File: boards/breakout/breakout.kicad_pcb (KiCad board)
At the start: 2 copper layers, 111 x 56 mm, 12 parts, among them J1 8P8C_Shielded, J2 DE15_Receptacle_HighDensity_M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, J3 Conn_02x04_Odd_Even, J4 Conn_02x05_Odd_Even

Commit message: Rev1 hardware
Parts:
- R1, R2: footprint Resistor_SMD:R_0805_2012Metric_Pad1.20x1.40mm_HandSolder -> Resistor_THT:R_Axial_DIN0204_L3.6mm_D1.6mm_P7.62mm_Horizontal
- moved R1 6.19 mm to (65.7, 37.7)
- moved R2 6.19 mm to (68.3, 37.7)
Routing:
- net Net-(D2-A): track 36.8 -> 31.7 mm
- net Net-(D1-A): track 31.2 -> 26.0 mm
- net /LEDA: track 18.5 -> 17.4 mm
- net /LEDB: track 16.9 -> 16.3 mm

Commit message: update schematics
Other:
- board text added: "1 2 3 4 5 6 7 8 9 10"
- board text added: "10"
- board text added: "2"
- board text added: "9"
- board text added: "Red Red Ground Sense 1 Composite Sync Green Sense 0 NC Green Ground Blue Blue Ground"
- board text added: "SEthernet Breakout github.com/rhalkyard/SEThernet Revision 1"
- board text removed: "SEthernet Breakout github.com/rhalkyard/SEThernet Revision 0"
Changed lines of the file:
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@@
   (gr_rect (start 30.95 23.5) (end 141.95 79.5)
     (stroke (width 0.1) (type default)) (fill none) (layer "Edge.Cuts"))
-  (gr_text "SEthernet" (at 46.99 39.49) (layer "B.SilkS")
+  (gr_text "2" (at 118.834 26.167) (layer "B.SilkS")
     (effects (font (size 1 1) (thickness 0.15)) (justify bottom mirror))
   )
-  (gr_text "RasterOps ColorBoard 264" (at 116.84 39.49) (layer "B.SilkS")
+  (gr_text "1" (at 120.104 36.327) (layer "B.SilkS")
+    (effects (font (size 1 1) (thickness 0.15)) (justify top mirror))
+  )
+  (gr_text "10" (at 108.674 26.167) (layer "B.SilkS")
     (effects (font (size 1 1) (thickness 0.15)) (justify bottom mirror))
   )
-  (gr_text "SEthernet Breakout\ngithub.com/rhalkyard/SEThernet\nRevision 0" (at 36.665 24.89 90) (layer "B.SilkS")
+  (gr_text "SEthernet" (at 62.7 27.31) (layer "B.SilkS")
+    (effects (font (size 1 1) (thickness 0.2) bold) (justify right bottom mirror))
+  )
+  (gr_text "RasterOps ColorBoard 264" (at 102.07 27.31) (layer "B.SilkS")
+    (effects (font (size 1 1) (thickness 0.2) bold) (justify left bottom mirror))
+  )
+  (gr_text "Red\nRed Ground\nSense 1\nComposite Sync\nGreen\nSense 0\nNC\nGreen Ground\nBlue\nBlue Ground" (at 98.895 28.58) (layer "B.SilkS")
+    (effects (font (size 1 1) (thickness 0.15)) (justify left top mirror))
+  )
+  (gr_text "1\n2\n3\n4\n5\n6\n7\n8\n9\n10" (at 102.07 28.58) (layer "B.SilkS")
+    (effects (font (size 1 1) (thickness 0.15)) (justify left top mirror))
+  )
+  (gr_text "SEthernet Breakout\ngithub.com/rhalkyard/SEThernet\nRevision 1" (at 36.665 24.89 90) (layer "B.SilkS")
     (effects (font (size 1 1) (thickness 0.15)) (justify left bottom mirror))
   )
+  (gr_text "9" (at 108.674 36.327) (layer "B.SilkS")
+    (effects (font (size 1 1) (thickness 0.15)) (justify top mirror))
+  )
   (gr_text "Link" (at 67.909 63.714) (layer "F.SilkS")

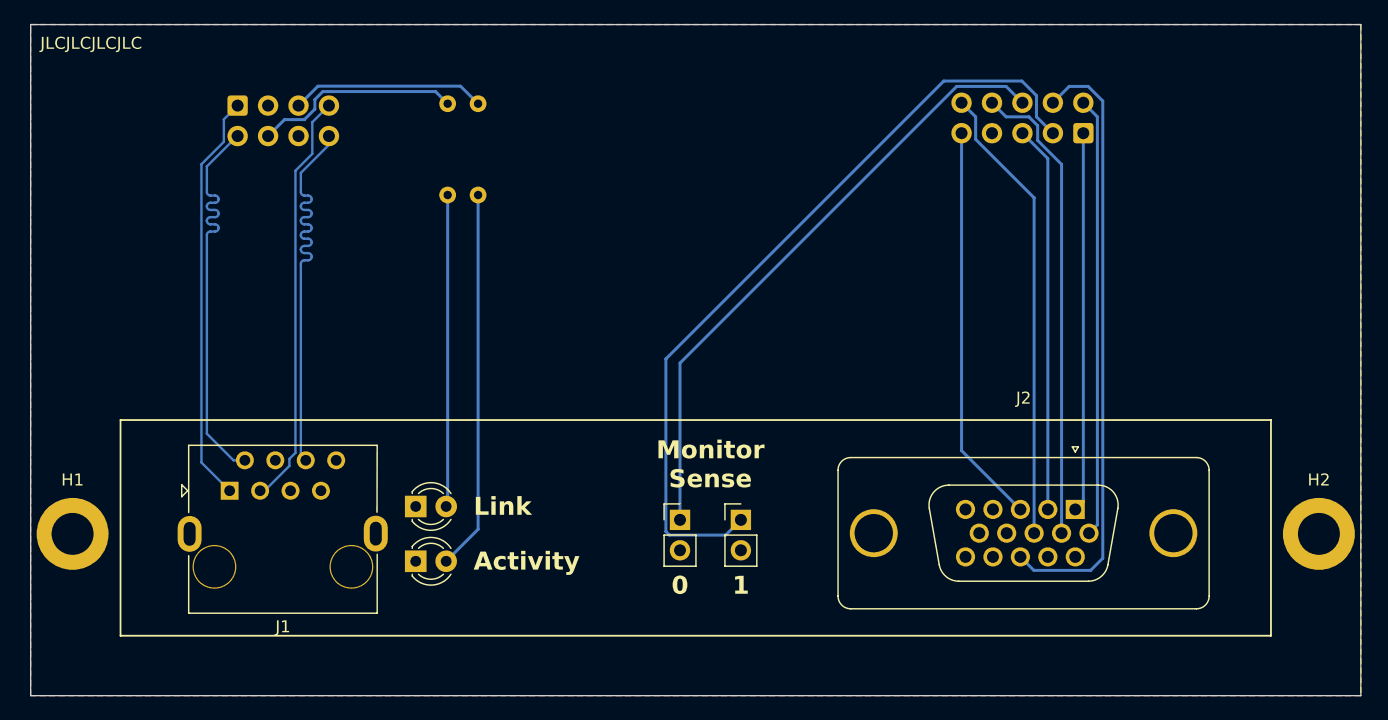
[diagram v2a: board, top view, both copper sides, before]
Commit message: Breakout: use threaded inserts for mounting
Resize mounting holes for use with Wurth 9774025360R threaded inserts.
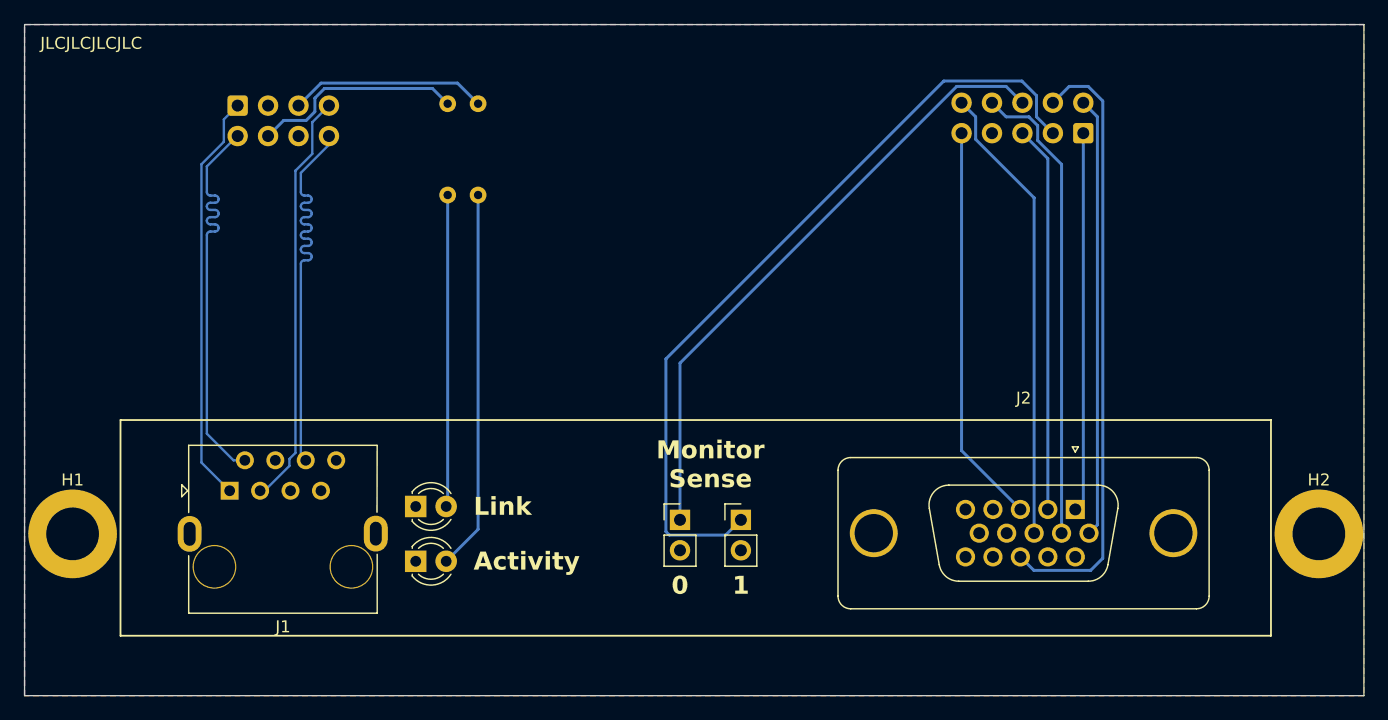
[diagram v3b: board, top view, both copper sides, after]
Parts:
- H1, H2: footprint PDS-Ethernet:MountingHole_3.5mm_Pad -> PDS-Ethernet:Wurth_9774025360R
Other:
- board size 111 x 56 mm -> 111.8 x 56 mm
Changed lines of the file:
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@@
     (property "Sheetfile" "breakout.kicad_sch")
     (property "Sheetname" "")
-    (property "ki_description" "Jumper, 2-pole, closed/bridged")
+    (property "ki_description" "Jumper, 2-pole, open")
     (property "ki_keywords" "Jumper SPST")
     (attr through_hole)
@@
     )
   )
-  (footprint "PDS-Ethernet:MountingHole_3.5mm_Pad" (layer "F.Cu")
+  (footprint "PDS-Ethernet:Wurth_9774025360R" (layer "F.Cu")
     (at 34.45 66)
     (descr "Mounting Hole 3.5mm")
@@
     (fp_circle (center 0 0) (end 3.25 0)
       (stroke (width 0.05) (type solid)) (fill none) (layer "F.CrtYd"))
-    (pad "1" thru_hole circle (at 0 0) (size 6 6) (drill 3.5) (layers "*.Cu" "*.Mask")
+    (pad "1" thru_hole circle (at 0 0) (size 7.4 7.4) (drill 4.4) (layers "*.Cu" "*.Mask")
       (net 1 "Earth") (pinfunction "1") (pintype "input"))
   )
@@
     )
   )
-  (footprint "PDS-Ethernet:MountingHole_3.5mm_Pad" (layer "F.Cu")
+  (footprint "PDS-Ethernet:Wurth_9774025360R" (layer "F.Cu")
     (at 138.45 66)
     (descr "Mounting Hole 3.5mm")
@@
     (fp_circle (center 0 0) (end 3.25 0)
       (stroke (width 0.05) (type solid)) (fill none) (layer "F.CrtYd"))
-    (pad "1" thru_hole circle (at 0 0) (size 6 6) (drill 3.5) (layers "*.Cu" "*.Mask")
+    (pad "1" thru_hole circle (at 0 0) (size 7.4 7.4) (drill 4.4) (layers "*.Cu" "*.Mask")
       (net 1 "Earth") (pinfunction "1") (pintype "input"))
   )
@@
     (property "Sheetfile" "breakout.kicad_sch")
     (property "Sheetname" "")
-    (property "ki_description" "Jumper, 2-pole, closed/bridged")
+    (property "ki_description" "Jumper, 2-pole, open")
     (property "ki_keywords" "Jumper SPST")
     (attr through_hole)
@@
     (descr "Resistor, Axial_DIN0204 series, Axial, Horizontal, pin pitch=7.62mm, 0.167W, length*diameter=3.6*1.6mm^2, http://cdn-reichelt.de/documents/datenblatt/B400/1_4W%23YAG.pdf")
     (tags "Resistor Axial_DIN0204 series Axial Horizontal pin pitch 7.62mm 0.167W length 3.6mm diameter 1.6mm")
-    (property "Digikey" "RMCF0805FT180R")
+    (property "Digikey" "CF18JT180R")
     (property "Sheetfile" "breakout.kicad_sch")
     (property "Sheetname" "")
@@
     (descr "Resistor, Axial_DIN0204 series, Axial, Horizontal, pin pitch=7.62mm, 0.167W, length*diameter=3.6*1.6mm^2, http://cdn-reichelt.de/documents/datenblatt/B400/1_4W%23YAG.pdf")
     (tags "Resistor Axial_DIN0204 series Axial Horizontal pin pitch 7.62mm 0.167W length 3.6mm diameter 1.6mm")
-    (property "Digikey" "RMCF0805FT180R")
+    (property "Digikey" "CF18JT180R")
     (property "Sheetfile" "breakout.kicad_sch")
     (property "Sheetname" "")
@@
   (gr_rect (start 38.45 56.5) (end 134.45 74.5)
     (stroke (width 0.15) (type default)) (fill none) (layer "F.SilkS"))
-  (gr_rect (start 30.95 23.5) (end 141.95 79.5)
+  (gr_rect (start 30.442 23.5) (end 142.204 79.5)
     (stroke (width 0.1) (type default)) (fill none) (layer "Edge.Cuts"))
   (gr_text "2" (at 118.834 26.167) (layer "B.SilkS")
@@
   (segment (start 115.831 34.6835) (end 115.831 63.961) (width 0.25) (layer "B.Cu") (net 3))
   (segment (start 113.711 32.5635) (end 115.831 34.6835) (width 0.25) (layer "B.Cu") (net 3))
-  (segment (start 66.825656 28.641656) (end 68.288 30.104) (width 0.25) (layer "B.Cu") (net 4))
-  (segment (start 53.302 30.262) (end 54.922344 28.641656) (width 0.25) (layer "B.Cu") (net 4))
-  (segment (start 54.922344 28.641656) (end 66.825656 28.641656) (width 0.25) (layer "B.Cu") (net 4))
+  (segment (start 55.179501 28.384499) (end 66.568499 28.384499) (width 0.25) (layer "B.Cu") (net 4))
+  (segment (start 66.568499 28.384499) (end 68.288 30.104) (width 0.25) (layer "B.Cu") (net 4))
+  (segment (start 53.302 30.262) (end 55.179501 28.384499) (width 0.25) (layer "B.Cu") (net 4))
   (segment (start 55.842 33.533) (end 53.496001 35.878999) (width 0.2) (layer "B.Cu") (net 5))
   (segment (start 53.496001 43.47) (end 53.496001 59.450001) (width 0.2) (layer "B.Cu") (net 5))
@@
   (segment (start 47.072 33.286) (end 47.072 31.412) (width 0.2) (layer "B.Cu") (net 8))
   (segment (start 45.203 60.047) (end 45.203 35.155) (width 0.2) (layer "B.Cu") (net 8))
-  (segment (start 50.762 32.802) (end 52.131656 31.432344) (width 0.25) (layer "B.Cu") (net 9))
-  (segment (start 53.79171 31.432344) (end 54.667 30.557054) (width 0.25) (layer "B.Cu") (net 9))
-  (segment (start 52.131656 31.432344) (end 53.79171 31.432344) (width 0.25) (layer "B.Cu") (net 9))
-  (segment (start 54.667 29.755) (end 55.330344 29.091656) (width 0.25) (layer "B.Cu") (net 9))
-  (segment (start 64.735656 29.091656) (end 65.748 30.104) (width 0.25) (layer "B.Cu") (net 9))
-  (segment (start 55.330344 29.091656) (end 64.735656 29.091656) (width 0.25) (layer "B.Cu") (net 9))
-  (segment (start 54.667 30.557054) (end 54.667 29.755) (width 0.25) (layer "B.Cu") (net 9))
+  (segment (start 53.937 31.501) (end 54.667 30.771) (width 0.25) (layer "B.Cu") (net 9))
+  (segment (start 54.667 30.771) (end 54.667 29.638149) (width 0.25) (layer "B.Cu") (net 9))
+  (segment (start 55.471149 28.834) (end 64.478 28.834) (width 0.25) (layer "B.Cu") (net 9))
+  (segment (start 50.762 32.802) (end 52.063 31.501) (width 0.25) (layer "B.Cu") (net 9))
+  (segment (start 64.478 28.834) (end 65.748 30.104) (width 0.25) (layer "B.Cu") (net 9))
+  (segment (start 52.063 31.501) (end 53.937 31.501) (width 0.25) (layer "B.Cu") (net 9))
+  (segment (start 54.667 29.638149) (end 55.471149 28.834) (width 0.25) (layer "B.Cu") (net 9))
   (segment (start 113.541 63.961) (end 108.631 59.051) (width 0.25) (layer "B.Cu") (net 10))
   (segment (start 108.631 59.051) (end 108.631 32.5635) (width 0.25) (layer "B.Cu") (net 10))
@@
     (polygon
       (pts
-        (xy 141.95 79.5)
-        (xy 30.95 79.5)
-        (xy 30.95 23.5)
-        (xy 141.95 23.5)
+        (xy 142.204 79.5)
+        (xy 30.442 79.5)
+        (xy 30.442 23.5)
+        (xy 142.204 23.5)
       )
     )
